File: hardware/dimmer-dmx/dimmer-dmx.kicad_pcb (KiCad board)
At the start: 2 copper layers, 68.6 x 53.3 mm, 34 parts, among them J1 Input, J2 XLR-3F-5F, J3 XLR-3M-5M, J4 Bypass, J5 Bypass, U1 NMA0505SC, U2 6N137, U3 6N137, U4 6N137, U5 MAX3485

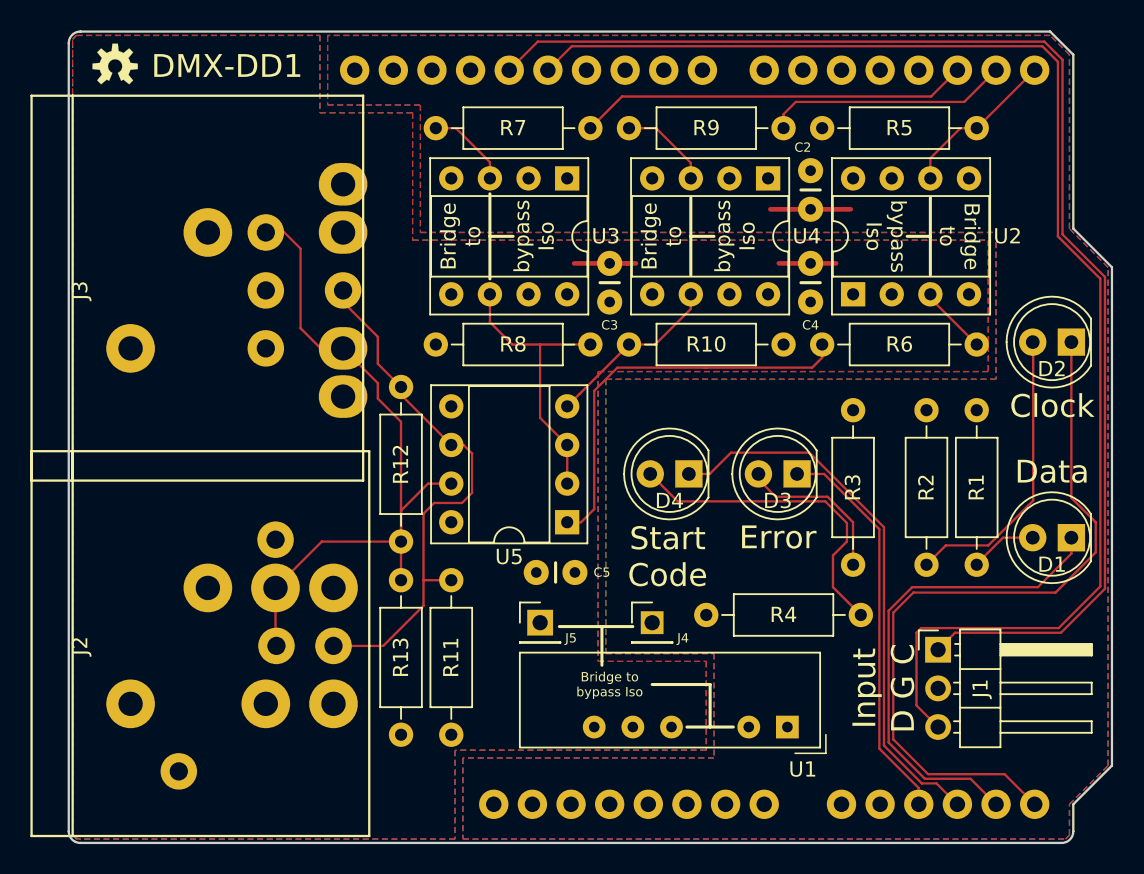
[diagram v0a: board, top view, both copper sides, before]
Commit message: Rev 1.1 DMX-DD1: - Move XLR connectors - Cleanup Iso bypass - Update parts list in README
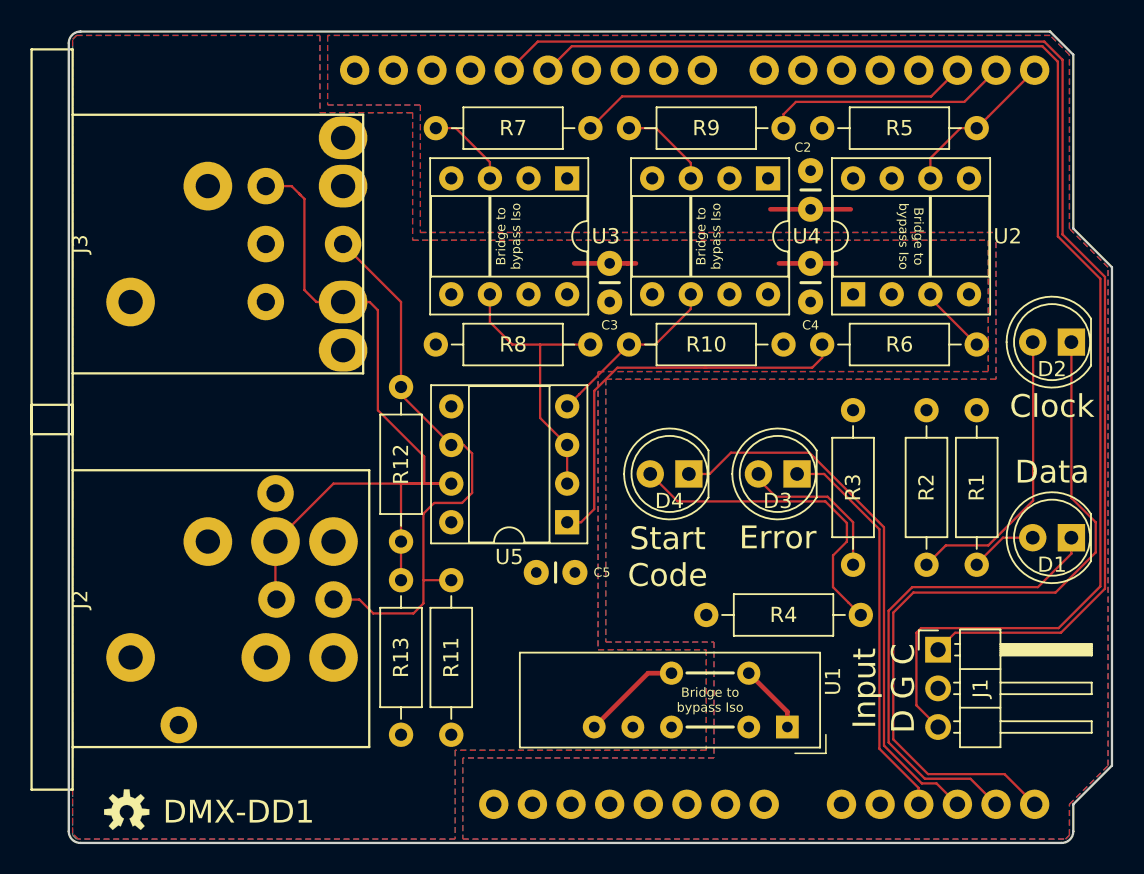
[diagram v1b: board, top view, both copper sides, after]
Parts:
- removed J4, J5: Bypass, Connector_PinHeader_2.54mm:PinHeader_1x01_P2.54mm_Vertical
- J2: value XLR-3F-5F -> NC3FAH/NC5FAH
- J3: value XLR-3M-5M -> NC3MAH/NC5MAH
- U1: footprint Converter_DCDC:Converter_DCDC_muRata_NMAxxxxSC_THT -> footprints:Converter_DCDC_muRata_NMAxxxxSC_THT_Bypass
- moved ? 49.0 mm to (120.1, 114.6)
- moved J2 3.05 mm to (116.6, 100.6)
- moved J3 3.05 mm to (116.6, 77.2)
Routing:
- net VDD: track 7.82 -> 14.4 mm
- net Net-(J2-Pad2A): track 47.5 -> 53.7 mm
- net +5V: track 5.28 -> 9.88 mm
- net Net-(J2-Pad3): track 36.2 -> 38.4 mm
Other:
- board text added: "DMX-DD1, Rev 1.1 Crazy Giraffe Software"
- board text removed: "DMX-DD1, Rev 1.0 Crazy Giraffe Software"
